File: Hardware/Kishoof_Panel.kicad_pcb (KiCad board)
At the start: 2 copper layers, 81 x 128.5 mm, 20 parts

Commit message: Rearranged Panel
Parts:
- removed the Ref** at (84.0, 118.0)
- added Ref**: Thonkiconn_Socket_MountingHole_6mm, Custom_Footprints:Thonkiconn_Socket_MountingHole_6mm, F.Cu at (111.0, 142.0)
- added Ref**: Alpha_9mm_pot_hole, Custom_Footprints:Alpha_9mm_pot_hole, F.Cu at (91.0, 117.0)
- added Ref**: Tall_Trimmer_Hole, Custom_Footprints:Tall_Trimmer_Hole, F.Cu at (73.0, 117.0)
- added Ref**: Tall_Trimmer_Hole, Custom_Footprints:Tall_Trimmer_Hole, F.Cu at (60.0, 117.0)
- added Ref**: Push_Button_Hole, Custom_Footprints:Small_Pushbutton_Hole_3.5mm, F.Cu at (109.0, 117.0)
- moved Ref** 47.5 mm to (71.0, 142.0)
- moved Ref** 46.9 mm to (91.0, 142.0)
- moved Ref** 37.4 mm to (91.0, 92.0)
- moved Ref** 27.0 mm to (101.0, 142.0)
- moved Ref** 18.4 mm to (104.0, 68.0)
- moved REF** 17.0 mm to (91.0, 132.0)
- moved Ref** 9.43 mm to (81.0, 142.0)
- moved Ref** 8.25 mm to (121.0, 68.0)
- moved Ref** 5.10 mm to (122.0, 117.0)
- moved Ref** 1.02 mm to (59.0, 142.0)
- moved Ref** 0.30 mm to (122.0, 142.0)
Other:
- board text added: "Oct"
- board text added: "Pitch"
- board text added: "Type"
- board text added: "VCA"
- board text added: "WTA"
- board text added: "WTB"
- board text added: "Wavetable A"
- board text added: "Wavetable B"
- board text removed: "1V/OCT"
- board text removed: "Bend"
- board text removed: "Channel A"
- board text removed: "Channel B"
- board text removed: "Mirror"
- board text removed: "Squeeze"
- board text removed: "Unison"
- board text removed: "WaveTable Pos"

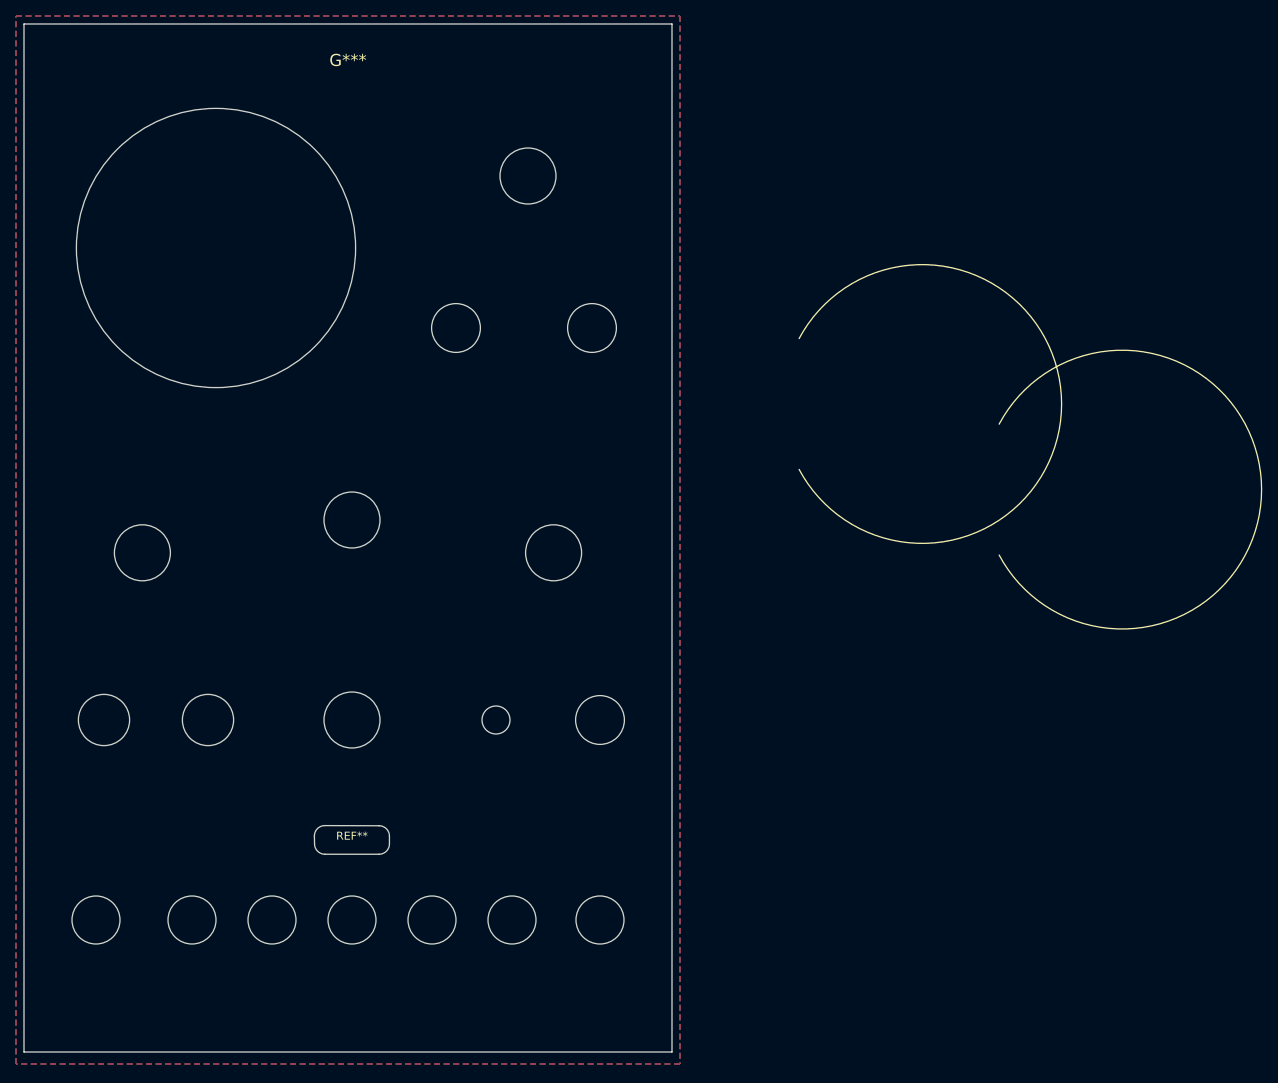
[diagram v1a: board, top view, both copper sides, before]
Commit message: Updating component and panel PCBs
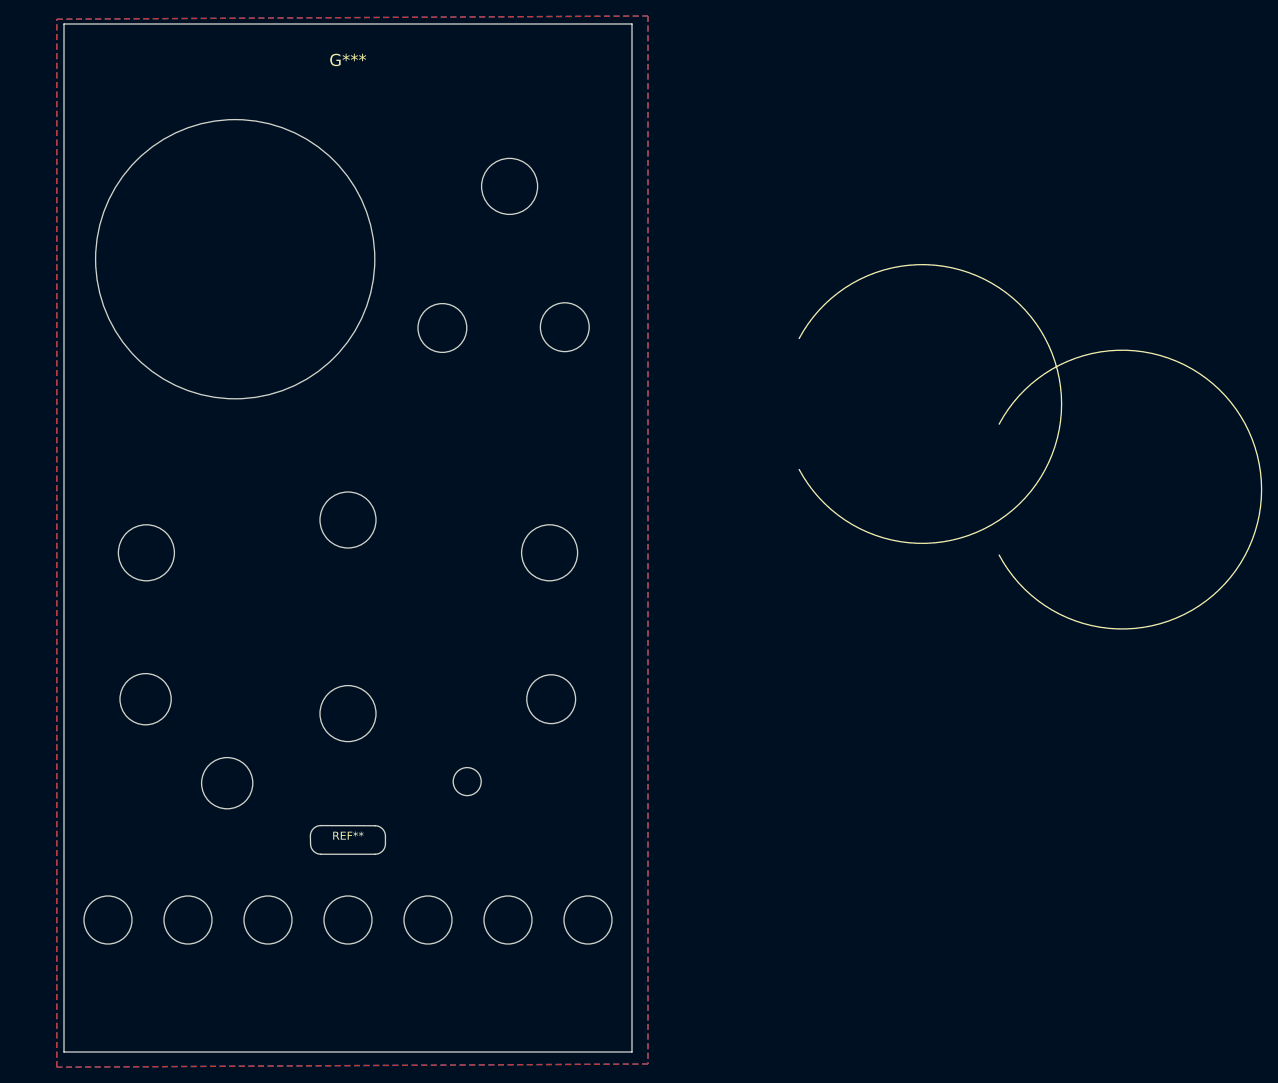
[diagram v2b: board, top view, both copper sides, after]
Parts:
- moved Ref** 8.50 mm to (105.4, 124.7)
- moved Ref** 8.26 mm to (75.4, 124.9)
- moved Ref** 6.63 mm to (115.9, 114.4)
- moved Ref** 5.81 mm to (65.2, 114.4)
- moved Ref** 5.00 mm to (62.5, 155.5)
- moved Ref** 5.00 mm to (118.5, 155.5)
- moved Ref** 5.00 mm to (62.5, 33.0)
- moved Ref** 5.00 mm to (118.5, 33.0)
- moved Ref** 3.40 mm to (117.6, 67.9)
- moved Ref** 2.64 mm to (110.7, 50.3)
- moved Ref** 1.70 mm to (102.3, 68.0)
- moved Ref** 1.50 mm to (60.5, 142.0)
- moved Ref** 1.50 mm to (120.5, 142.0)
- moved Ref** 0.94 mm to (90.5, 116.2)
- moved REF** 0.50 mm to (90.5, 132.0)
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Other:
- board size 81 x 128.5 mm -> 71 x 128.5 mm
- board text added: "RM"
- board text removed: "Ring Mod"
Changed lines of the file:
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@@
 	(footprint "Custom_Footprints:Thonkiconn_Socket_MountingHole_6mm"
 		(layer "F.Cu")
-		(at 111 142)
+		(at 110.5 142)
 		(descr "Mounting Hole 6mm, no annular")
 		(tags "mounting hole 6mm no annular")
@@
 	(footprint "Custom_Footprints:MountingHole_6.1mm"
 		(layer "F.Cu")
-		(at 122 117)
+		(at 115.9 114.4)
 		(descr "Mounting Hole 6mm, no annular")
 		(tags "mounting hole 6mm no annular")
@@
 	(footprint "Custom_Footprints:Tall_Trimmer_Hole"
 		(layer "F.Cu")
-		(at 73 117)
+		(at 75.4 124.9)
 		(descr "Mounting Hole 6.5mm")
 		(tags "mounting hole 6.5mm")
@@
 	(footprint "Custom_Footprints:Tall_Trimmer_Hole"
 		(layer "F.Cu")
-		(at 60 117)
+		(at 65.2 114.4)
 		(descr "Mounting Hole 6.5mm")
 		(tags "mounting hole 6.5mm")
@@
 	(footprint "Custom_Footprints:MountingHole_6.1mm"
 		(layer "F.Cu")
-		(at 121 68)
+		(at 117.6 67.9)
 		(descr "Mounting Hole 6mm, no annular")
 		(tags "mounting hole 6mm no annular")
@@
 	(footprint "Custom_Footprints:Thonkiconn_Socket_MountingHole_6mm"
 		(layer "F.Cu")
-		(at 81 142)
+		(at 80.5 142)
 		(descr "Mounting Hole 6mm, no annular")
 		(tags "mounting hole 6mm no annular")
@@
 	(footprint "Custom_Footprints:Small_Pushbutton_Hole_3.5mm"
 		(layer "F.Cu")
-		(at 109 117)
+		(at 105.4 124.7)
 		(descr "Button Hole 3.5mm")
 		(property "Reference" "Ref**"
@@
 		(locked yes)
 		(layer "F.Cu")
-		(at 123.5 33)
+		(at 118.5 33)
 		(descr "Mounting Hole 6mm, no annular")
 		(tags "mounting hole 6mm no annular")
@@
 	(footprint "Custom_Footprints:Alpha_9mm_pot_hole"
 		(layer "F.Cu")
-		(at 116.2 96.1)
+		(at 115.7 96.1)
 		(descr "Mounting Hole 7mm")
 		(tags "mounting hole 7mm")
@@
 	(footprint "Custom_Footprints:Thonkiconn_Socket_MountingHole_6mm"
 		(layer "F.Cu")
-		(at 71 142)
+		(at 70.5 142)
 		(descr "Mounting Hole 6mm, no annular")
 		(tags "mounting hole 6mm no annular")
@@
 	(footprint "Custom_Footprints:Alpha_9mm_pot_hole"
 		(layer "F.Cu")
-		(at 91 92)
+		(at 90.5 92)
 		(descr "Mounting Hole 7mm")
 		(tags "mounting hole 7mm")
@@
 	(footprint "Custom_Footprints:Alpha_9mm_pot_hole"
 		(layer "F.Cu")
-		(at 113 49)
+		(at 110.7 50.3)
 		(descr "Mounting Hole 7mm")
 		(tags "mounting hole 7mm")
@@
 		(locked yes)
 		(layer "F.Cu")
-		(at 57.5 155.5)
+		(at 62.5 155.5)
 		(descr "Mounting Hole 6mm, no annular")
 		(tags "mounting hole 6mm no annular")
@@
 	(footprint "Custom_Footprints:Thonkiconn_Socket_MountingHole_6mm"
 		(layer "F.Cu")
-		(at 91 142)
+		(at 90.5 142)
 		(descr "Mounting Hole 6mm, no annular")
 		(tags "mounting hole 6mm no annular")
@@
 	(footprint "Custom_Footprints:MountingHole_6.1mm"
 		(layer "F.Cu")
-		(at 104 68)
+		(at 102.3 68)
 		(descr "Mounting Hole 6mm, no annular")
 		(tags "mounting hole 6mm no annular")
@@
 	(footprint "Custom_Footprints:Alpha_9mm_pot_hole"
 		(layer "F.Cu")
-		(at 91 117)
+		(at 90.5 116.2)
 		(descr "Mounting Hole 7mm")
 		(tags "mounting hole 7mm")
@@
 		(locked yes)
 		(layer "F.Cu")
-		(at 123.5 155.5)
+		(at 118.5 155.5)
 		(descr "Mounting Hole 6mm, no annular")
 		(tags "mounting hole 6mm no annular")
@@
 	(footprint "Custom_Footprints:Alpha_9mm_pot_hole"
 		(layer "F.Cu")
-		(at 64.8 96.1)
+		(at 65.3 96.1)
 		(descr "Mounting Hole 7mm")
 		(tags "mounting hole 7mm")
@@
 	(footprint "Custom_Footprints:USB_C_Cutout"
 		(layer "F.Cu")
-		(at 91 132)
+		(at 90.5 132)
 		(property "Reference" "REF**"
 			(at 0 -0.5 0)
@@
 	(footprint "Custom_Footprints:Thonkiconn_Socket_MountingHole_6mm"
 		(layer "F.Cu")
-		(at 59 142)
+		(at 60.5 142)
 		(descr "Mounting Hole 6mm, no annular")
 		(tags "mounting hole 6mm no annular")
@@
 	(footprint "Custom_Footprints:Thonkiconn_Socket_MountingHole_6mm"
 		(layer "F.Cu")
-		(at 122 142)
+		(at 120.5 142)
 		(descr "Mounting Hole 6mm, no annular")
 		(tags "mounting hole 6mm no annular")
@@
 		(locked yes)
 		(layer "F.Cu")
-		(at 57.5 33)
+		(at 62.5 33)
 		(descr "Mounting Hole 6mm, no annular")
 		(tags "mounting hole 6mm no annular")
@@
 	(footprint "Custom_Footprints:Thonkiconn_Socket_MountingHole_6mm"
 		(layer "F.Cu")
-		(at 101 142)
+		(at 100.5 142)
 		(descr "Mounting Hole 6mm, no annular")
 		(tags "mounting hole 6mm no annular")
@@
 	)
 	(gr_circle
-		(center 91 117)
-		(end 98.778175 117)
+		(center 90.5 116.2)
+		(end 98.278175 116.2)
 		(stroke
 			(width 0.15)
@@
 	)
 	(gr_circle
-		(center 113 49)
-		(end 120.778175 49)
+		(center 110.7 50.3)
+		(end 118.478175 50.3)
 		(stroke
 			(width 0.15)
@@
 	)
 	(gr_line
-		(start 71 142)
-		(end 60 117)
+		(start 70.5 142)
+		(end 65.2 114.2)
 		(stroke
-			(width 2)
+			(width 1)
 			(type default)
 		)
@@
 	)
 	(gr_circle
-		(center 73 117)
-		(end 77 117)
+		(center 75.4 124.9)
+		(end 79.4 124.9)
 		(stroke
 			(width 0.15)
@@
 	)
 	(gr_circle
-		(center 64.8 96.1)
-		(end 72.578175 96.1)
+		(center 65.3 96.1)
+		(end 73.078175 96.1)
 		(stroke
 			(width 0.15)
@@
 	)
 	(gr_circle
-		(center 109 117)
-		(end 111.778175 117)
+		(center 105.4 124.7)
+		(end 108.178175 124.7)
 		(stroke
 			(width 0.15)
@@
 	)
 	(gr_line
-		(start 74 58)
-		(end 113 49)
+		(start 76.1 59.1)
+		(end 110.4 50.2)
 		(stroke
 			(width 4)
@@
 	)
 	(gr_line
-		(start 73 117)
-		(end 91 117)
+		(start 75.4 124.7)
+		(end 90.5 117)
 		(stroke
-			(width 2)
+			(width 1)
 			(type default)
 		)
@@
 	)
 	(gr_circle
-		(center 60 117)
-		(end 64 117)
+		(center 65.2 114.4)
+		(end 69.2 114.4)
 		(stroke
 			(width 0.15)
@@
 	)
 	(gr_rect
-		(start 54 137)
-		(end 64 147)
+		(start 56.5 137.4)
+		(end 64.5 146.6)
 		(stroke
 			(width 2)
@@
 	)
 	(gr_line
-		(start 65 96.25)
-		(end 60 117)
+		(start 65.3 96.1)
+		(end 65.3 114.3)
 		(stroke
-			(width 2)
+			(width 1)
 			(type default)
 		)
@@
 	)
 	(gr_line
-		(start 81 142)
-		(end 73 117)
+		(start 80.5 142)
+		(end 77 124.7)
 		(stroke
-			(width 2)
+			(width 1)
 			(type default)
 		)
@@
 	)
 	(gr_circle
-		(center 74 58)
-		(end 93 59)
+		(center 76.4 59.4)
+		(end 95.4 60.4)
 		(stroke
 			(width 0.15)
@@
 	)
 	(gr_circle
-		(center 116.2 96.2)
-		(end 123.978175 96.2)
+		(center 115.7 96.2)
+		(end 123.478175 96.2)
 		(stroke
 			(width 0.15)
@@
 	)
 	(gr_rect
-		(start 117 137)
-		(end 127 147)
+		(start 116.55 137.5)
+		(end 124.45 146.5)
 		(stroke
 			(width 2)
@@
 	)
 	(gr_line
-		(start 91 117)
-		(end 91 92)
+		(start 90.6 116.9)
+		(end 90.5 91.9)
 		(stroke
-			(width 2)
+			(width 1)
 			(type default)
 		)
@@
 	)
 	(gr_circle
-		(center 91 92)
-		(end 98.778175 92)
+		(center 90.5 92)
+		(end 98.278175 92)
 		(stroke
 			(width 0.15)
@@
 	)
 	(gr_circle
-		(center 74 58)
-		(end 91.45 58)
+		(center 76.4 59.4)
+		(end 93.85 59.4)
 		(stroke
 			(width 0.05)
@@
 	)
 	(gr_rect
-		(start 50 30)
-		(end 131 158.5)
-		(locked yes)
+		(start 55 30)
+		(end 126 158.5)
 		(stroke
 			(width 0.1)
@@
 	)
 	(gr_text "Wavetable A"
-		(at 64 86 0)
+		(at 65.3 85.9 0)
 		(layer "F.Mask")
 		(effects
@@
 	)
 	(gr_text "OUT B"
-		(at 122 152 0)
+		(at 120.5 151 0)
 		(layer "F.Mask")
 		(effects
@@
 	)
 	(gr_text "Oct"
-		(at 109 123 0)
+		(at 105.4 130.7 0)
 		(layer "F.Mask")
 		(effects
@@
 		)
 	)
-	(gr_text "Ring Mod"
-		(at 122 125 0)
+	(gr_text "RM"
+		(at 115.9 122.4 0)
 		(layer "F.Mask")
 		(effects
@@
 	)
 	(gr_text "Octave"
-		(at 104 75 0)
+		(at 102.3 75 0)
 		(layer "F.Mask")
 		(effects
@@
 	)
 	(gr_text "Stepped"
-		(at 121 75 0)
+		(at 117.6 74.9 0)
 		(layer "F.Mask")
 		(effects
@@
 	)
 	(gr_text "Smooth"
-		(at 121 63 0)
+		(at 117.6 62.9 0)
 		(layer "F.Mask")
 		(effects
@@
 	)
 	(gr_text "WTA"
-		(at 71 151 0)
+		(at 71.2 151 0)
 		(layer "F.Mask")
 		(effects
@@
 	)
 	(gr_text "Type"
-		(at 91 82 0)
+		(at 90.5 82.2 0)
 		(layer "F.Mask")
 		(effects
@@
 	)
 	(gr_text "Mix"
-		(at 122 111 0)
+		(at 115.9 108.6 0)
 		(layer "F.Mask")
 		(effects
@@
 	)
 	(gr_text "Warp"
-		(at 81 151 0)
+		(at 81.1 151 0)
 		(layer "F.Mask")
 		(effects
@@
 	)
 	(gr_text "OUT A"
-		(at 59 152 0)
+		(at 60.5 151.1 0)
 		(layer "F.Mask")
 		(effects
@@
 	)
 	(gr_text "WTB"
-		(at 111 151 0)
+		(at 110.8 151 0)
 		(layer "F.Mask")
 		(effects
@@
 	)
 	(gr_text "Pitch"
-		(at 101 151 0)
+		(at 100.9 151 0)
 		(layer "F.Mask")
 		(effects
@@
 		(net 0)
 		(net_name "")
-		(locked yes)
 		(layers "F&B.Cu")
 		(hatch edge 0.508)
@@
 		(polygon
 			(pts
-				(xy 132 160) (xy 49 160) (xy 49 29) (xy 132 29)
+				(xy 128 160) (xy 54.1 160.4) (xy 54.1 29.4) (xy 128 29)
 			)
 		)

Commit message: First draft signal routing on component pcb
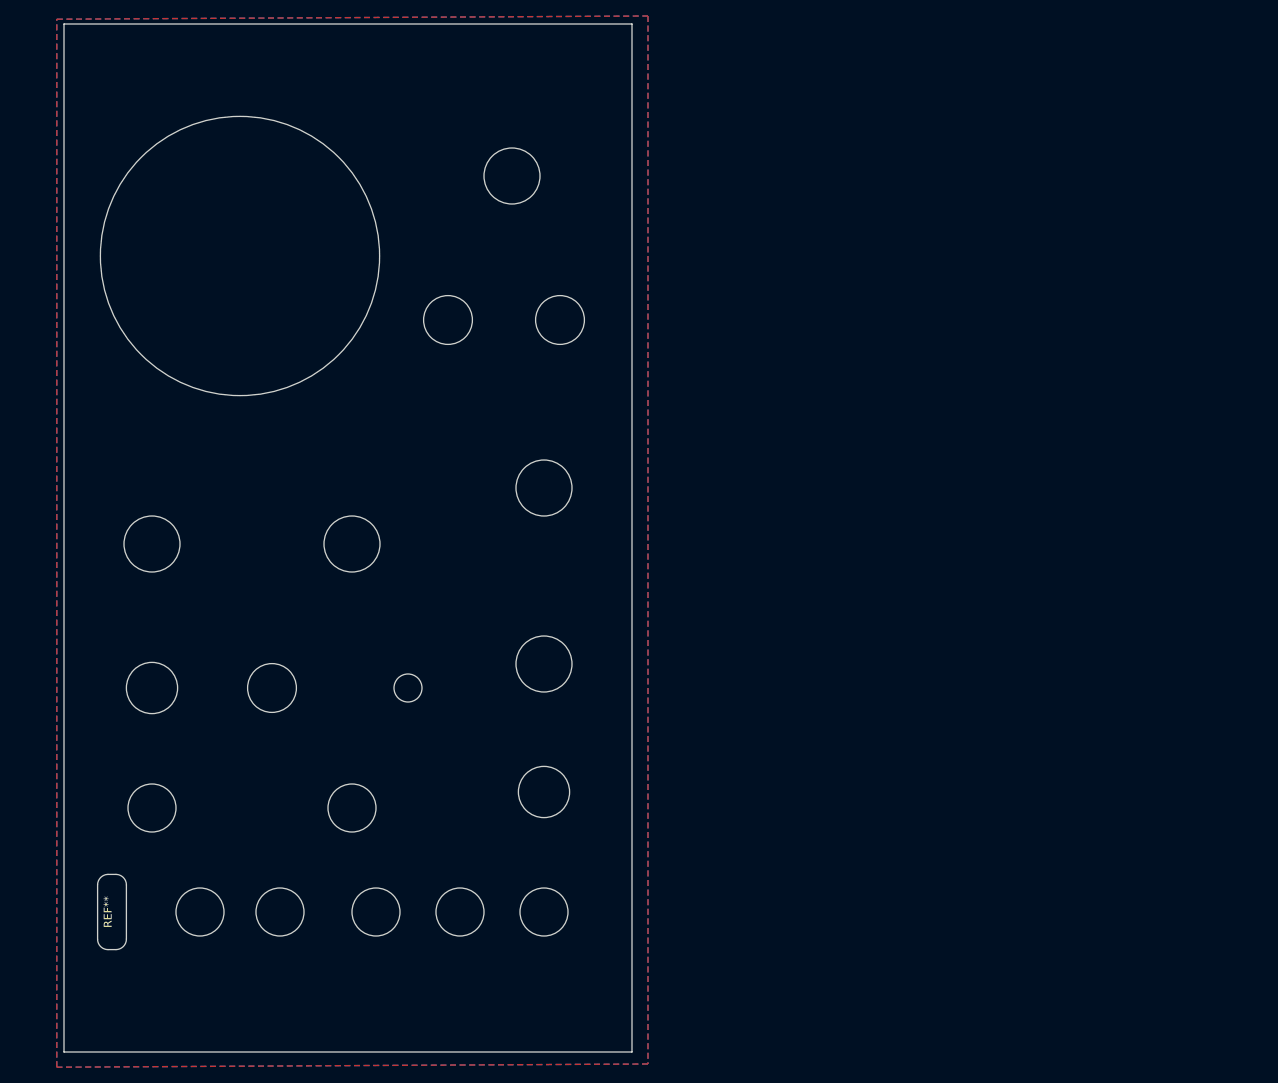
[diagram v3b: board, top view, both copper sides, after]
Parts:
- added G***: LOGO, Graphics:usb_icon, F.Cu at (61.0, 148.8)
- moved Ref** 39.6 mm to (115.0, 126.0)
- moved Ref** 34.9 mm to (81.0, 113.0)
- moved REF** 30.8 mm to (61.0, 141.0), turned to 90 degrees
- moved Ref** 25.3 mm to (115.0, 110.0)
- moved Ref** 24.8 mm to (115.0, 88.0)
- moved Ref** 24.7 mm to (91.0, 95.0)
- moved Ref** 24.0 mm to (91.0, 128.0)
- moved Ref** 15.0 mm to (66.0, 128.0)
- moved Ref** 13.8 mm to (98.0, 113.0)
- moved Ref** 5.59 mm to (115.0, 141.0)
- moved Ref** 4.12 mm to (104.5, 141.0)
- moved Ref** 3.64 mm to (94.0, 141.0)
- moved Ref** 1.80 mm to (72.0, 141.0)
- moved Ref** 1.80 mm to (82.0, 141.0)
- moved Ref** 1.61 mm to (66.0, 113.0)
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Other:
- outline, holes or cut-outs redrawn
- board text added: "A OUT B"
- board text added: "A Wavetable B"
- board text added: "PITCH"
- board text added: "Transpose"
- board text added: "WARP"
- board text added: "Warp Type"
- board text removed: "Mix"
- board text removed: "OUT A"
- board text removed: "OUT B"
- board text removed: "Octave"
- board text removed: "Pitch"
- board text removed: "RM"
- board text removed: "Smooth"
- board text removed: "Stepped"
- board text removed: "Type"
- board text removed: "WTA"
- board text removed: "WTB"
- board text removed: "Warp"
- board text removed: "Wavetable A"
- board text removed: "Wavetable B"
